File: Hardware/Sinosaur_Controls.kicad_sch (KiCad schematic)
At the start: 35 parts, among them J1 Conn_01x12_Male, J10 Sine1InvOut, J11 FM2Out, J12 FM3Out, J13 SwellOut, J14 ClockIn, J2 Conn_01x12_Male, J3 Conn_01x16_Male, J4 Conn_01x16_Male, J5 Sine1Out, J6 Sine2Out, J7 Sine3Out, J8 RampOut, J9 GateIn

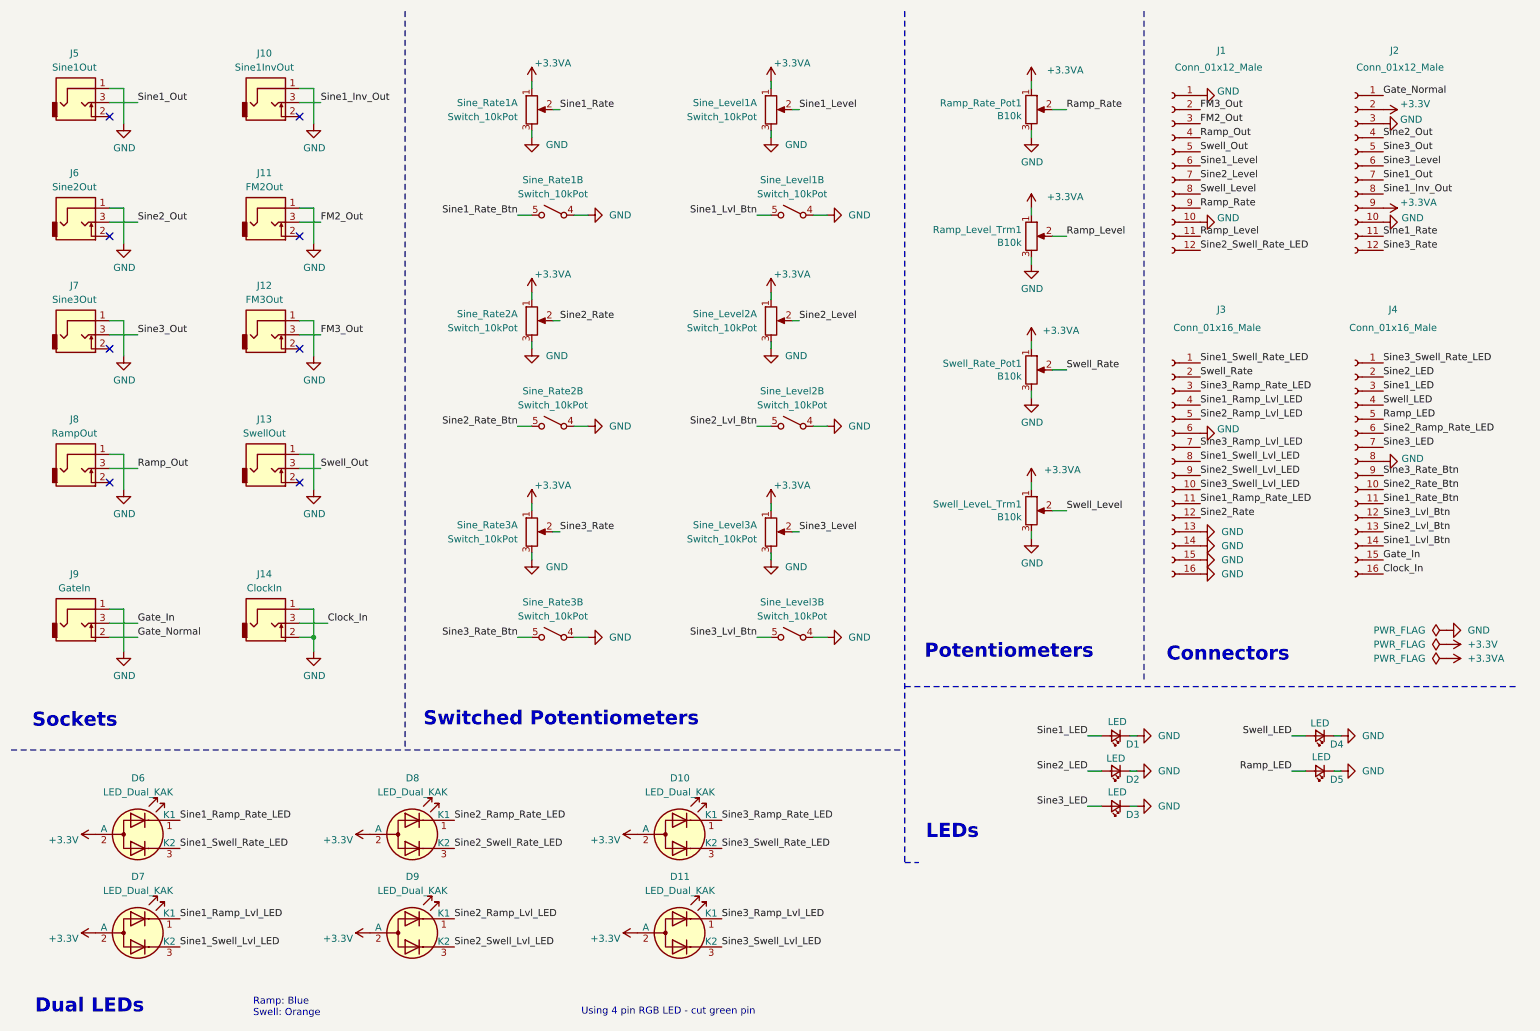
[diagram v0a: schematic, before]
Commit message: Added REadme; code cleanup
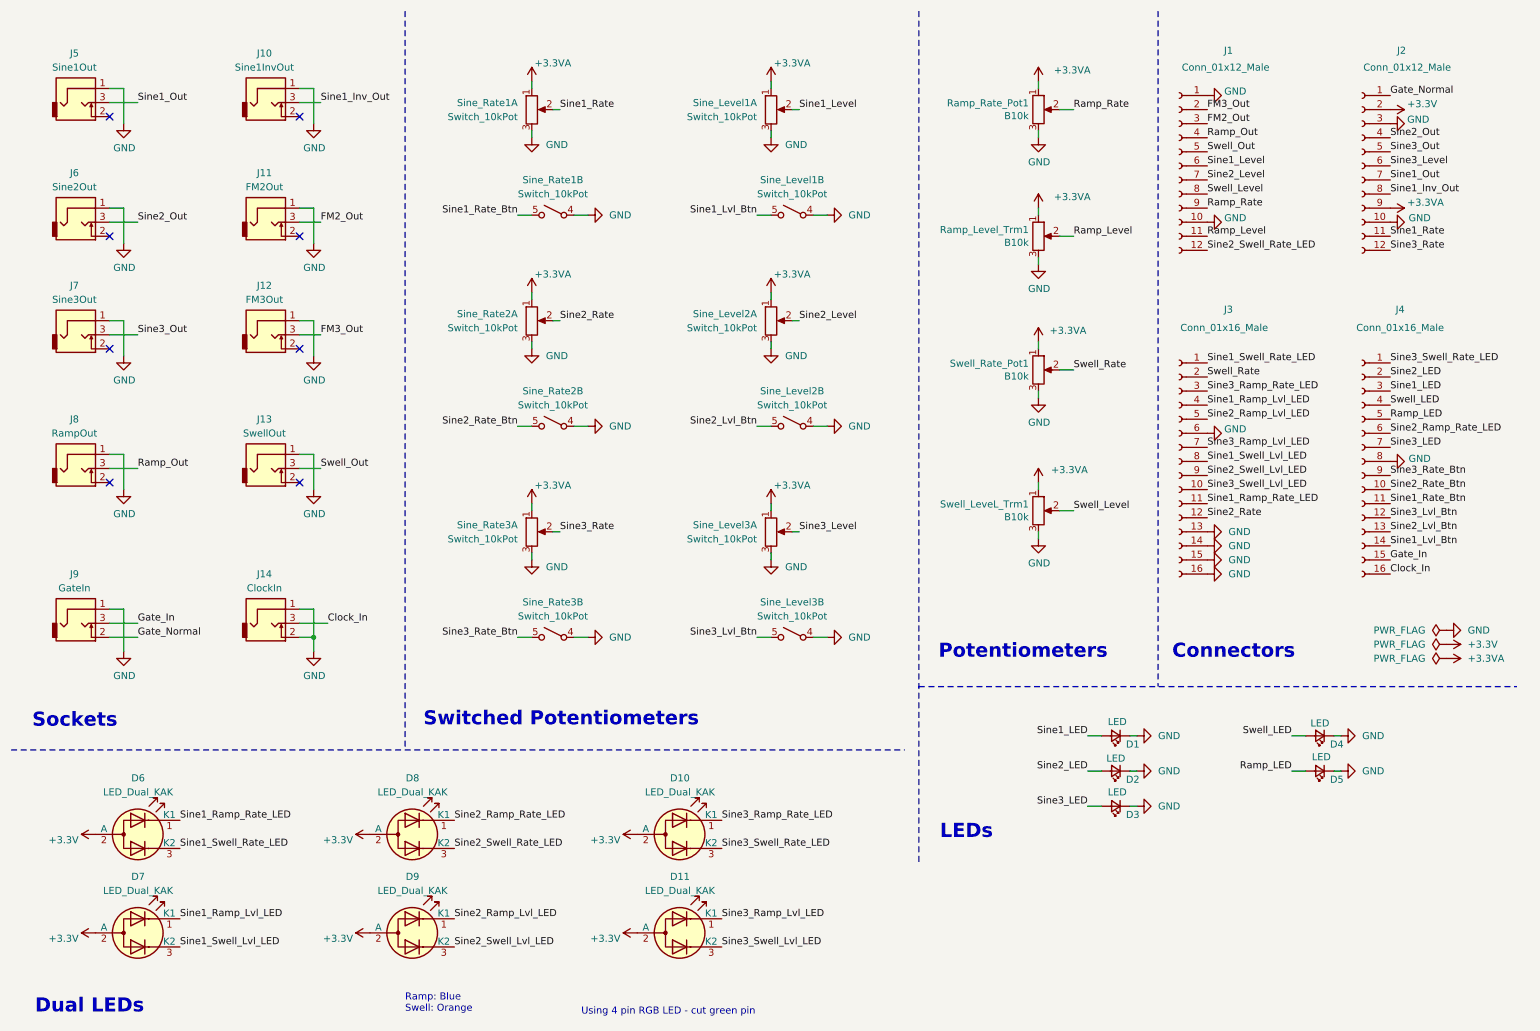
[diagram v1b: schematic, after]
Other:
- moved on the sheet: J1, J2, J3, J4, Ramp_Level_Trm1, Ramp_Rate_Pot1, Swell_LeveL_Trm1, Swell_Rate_Pot1
